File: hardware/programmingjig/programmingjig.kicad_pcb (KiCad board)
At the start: 2 copper layers, 17.9 x 28.3 mm, 15 parts, among them J1 SPGM, J11 PGMIO, J2 USB_C_Receptacle_USB2.0, J3 PGMVDD, J4 PGMO, J5 PGMVDD-POGO-5.5mm, U2 RS3236-3.3YUTDN4, U3 CH32V003JxMx

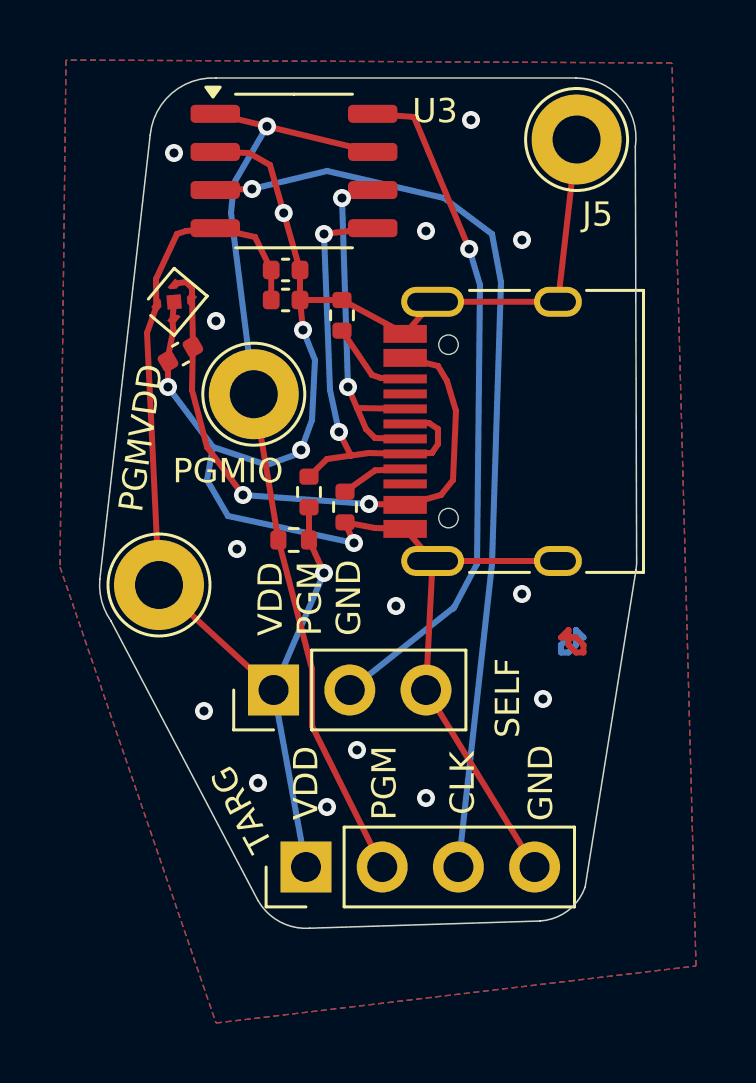
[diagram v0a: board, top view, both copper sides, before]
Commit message: Add firmware for programming jig
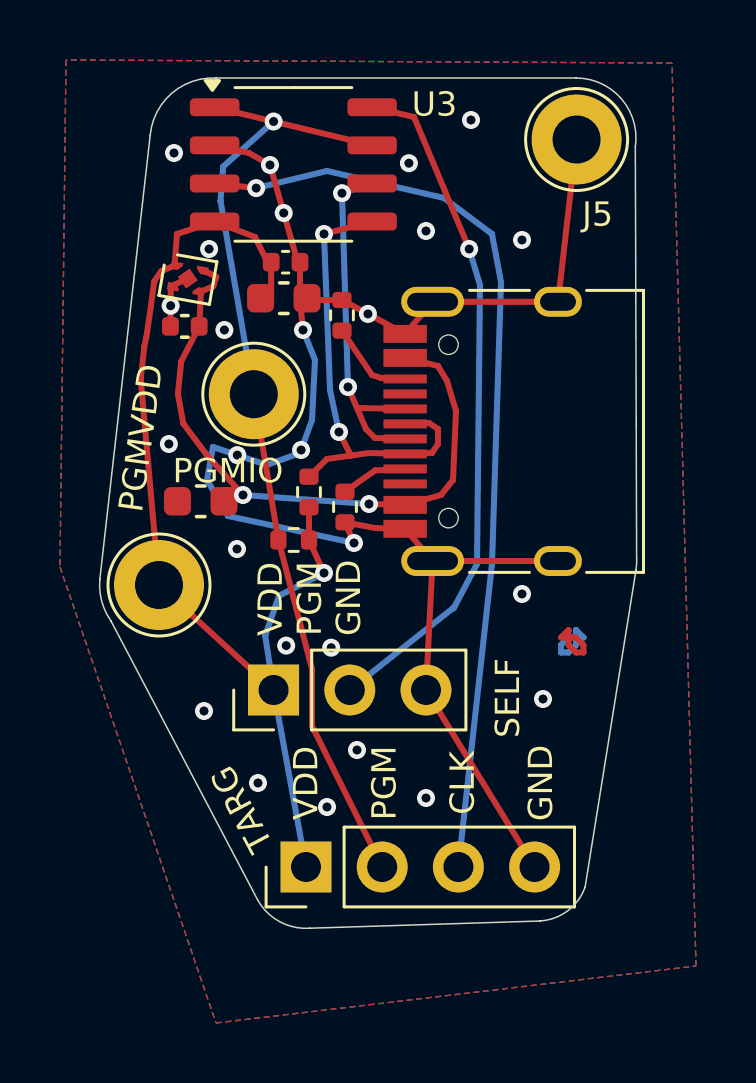
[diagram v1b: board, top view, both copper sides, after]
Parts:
- removed C6: 4.7u10v, Capacitor_SMD:C_0402_1005Metric
- added C3: 10u, Capacitor_SMD:C_0603_1608Metric, F.Cu at (158.5, 89.2)
- added C4: 1u25v, Capacitor_SMD:C_0402_1005Metric, F.Cu at (158.0, 83.4)
- C2: value 4.7u10v -> 10u; footprint Capacitor_SMD:C_0402_1005Metric -> Capacitor_SMD:C_0603_1608Metric
- moved U2 0.90 mm to (158.1, 81.8), turned to -100 degrees
- moved C1 0.26 mm to (161.3, 81.2)
- moved U3 0.22 mm to (161.6, 78.0)
- moved C2 0.08 mm to (161.3, 82.4)
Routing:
- net GND: track 61.5 -> 58.1 mm, vias 19 -> 26
- net VDD: track 34.5 -> 35.5 mm
- net VBUS: track 20.3 -> 21.2 mm
- net SLPGM: track 31.2 -> 31.9 mm
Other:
- board text added: "badderapple programmingjig ch32v003 rev A"
- board text removed: "badderapple programmingjig ch32v003 rev -"
